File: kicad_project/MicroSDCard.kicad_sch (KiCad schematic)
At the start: 8 parts, among them J8 DM3AT, U14 ADG733BRU, U6 BD2221G-LBTR

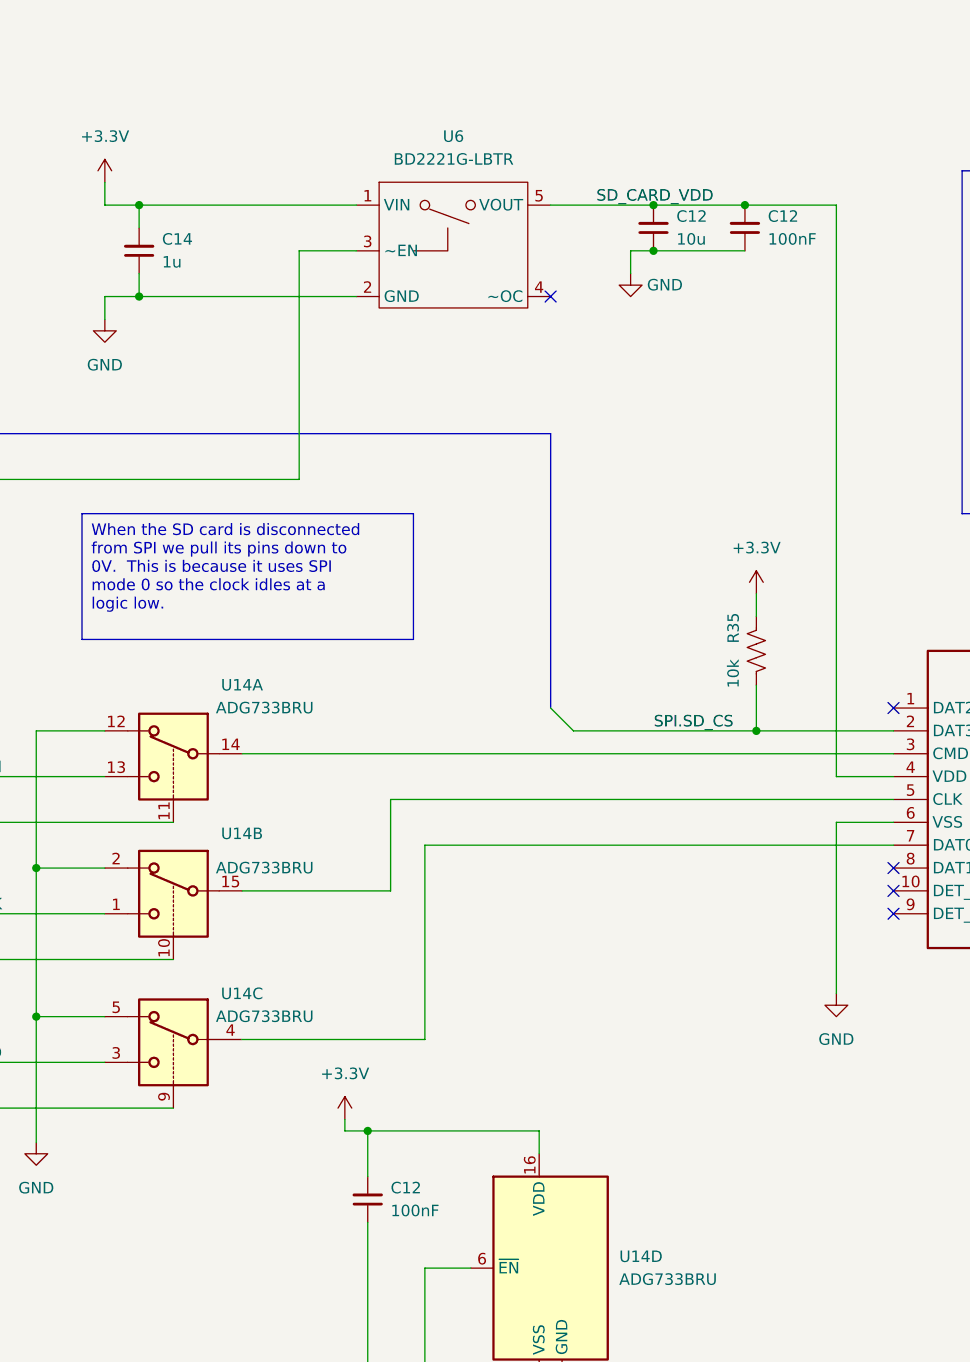
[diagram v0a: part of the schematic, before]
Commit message: Update to KiCAD 8, start adding CAN transceiver
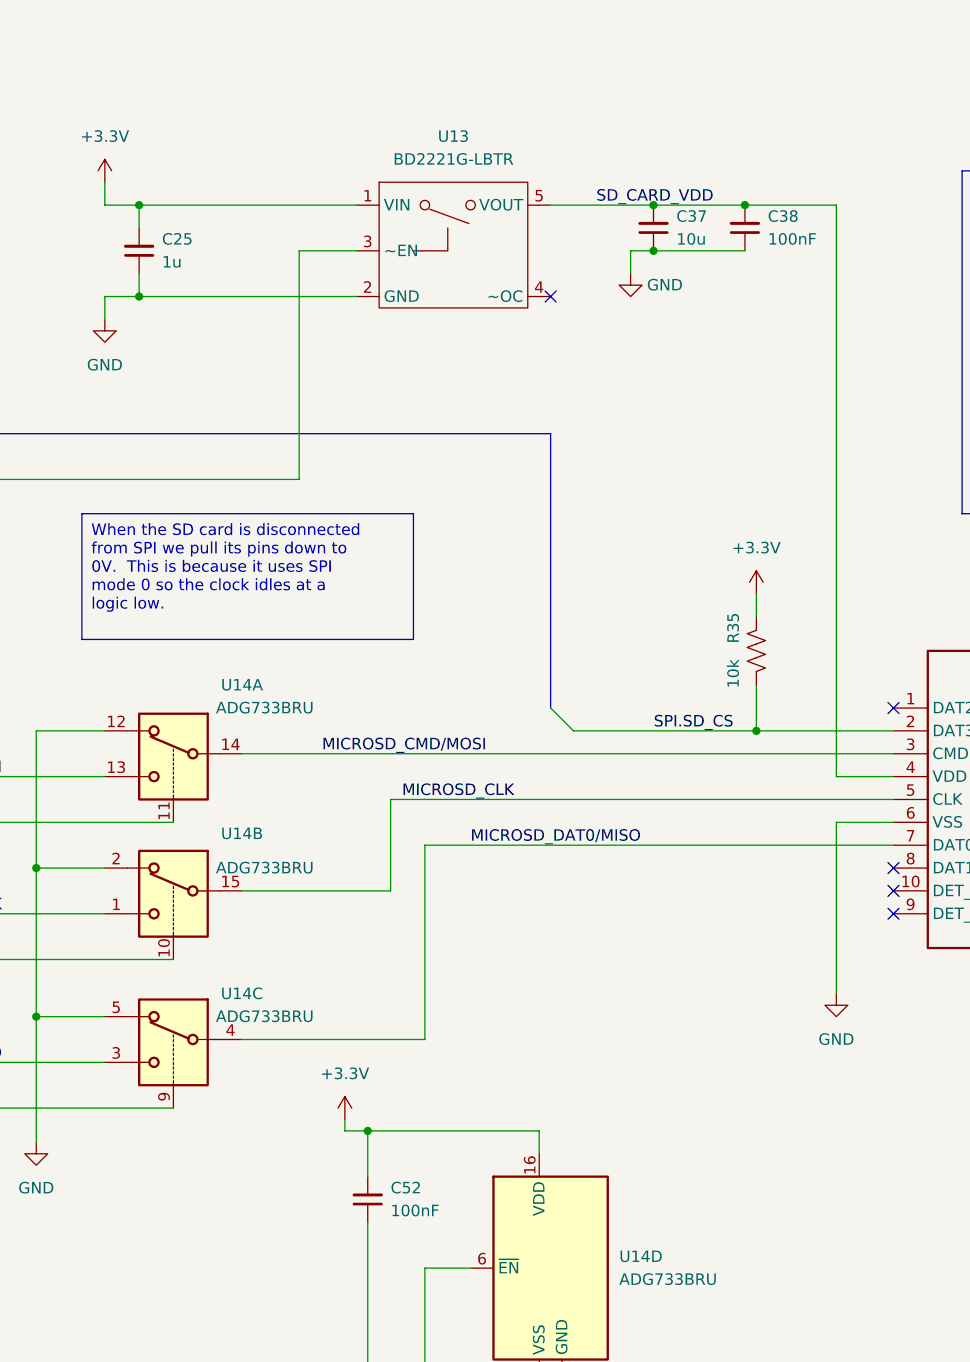
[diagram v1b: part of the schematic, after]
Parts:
- renumbered C14 to C25, C12 to C37, C12 to C38, C12 to C52, U6 to U13
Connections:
- net MICROSD_CMD/MOSI: now reaches J8.3 (CMD), U14.14
- net MICROSD_CLK: now reaches J8.5 (CLK), U14.15
- net MICROSD_DAT0/MISO: now reaches J8.7 (DAT0), U14.4

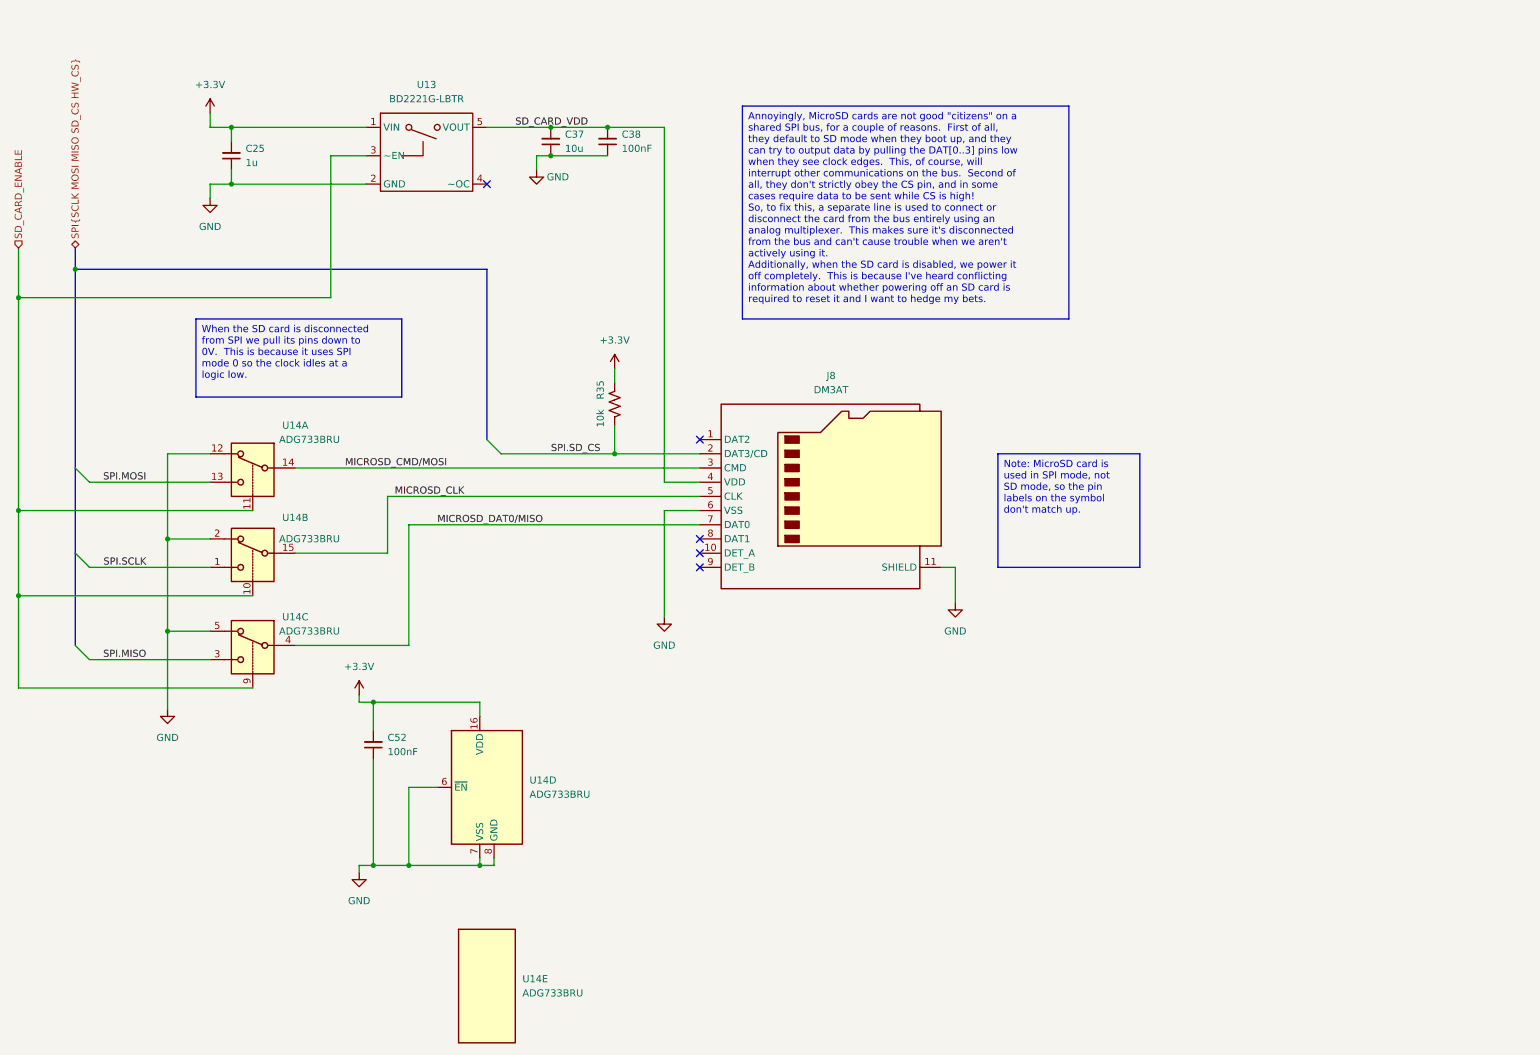
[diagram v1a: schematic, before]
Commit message: Fix all known issues with v2 r2: * Invert polarity of SD card enable line to match power switch * Decrease SPI mirror resistor resistance * Pull up SD card MISO line to 3V3 * Fix reset voltage divider to output 3.3V instead of 4V * Add diode to keep reset low while power is unplugged * Move analog in to A3 instead of A0
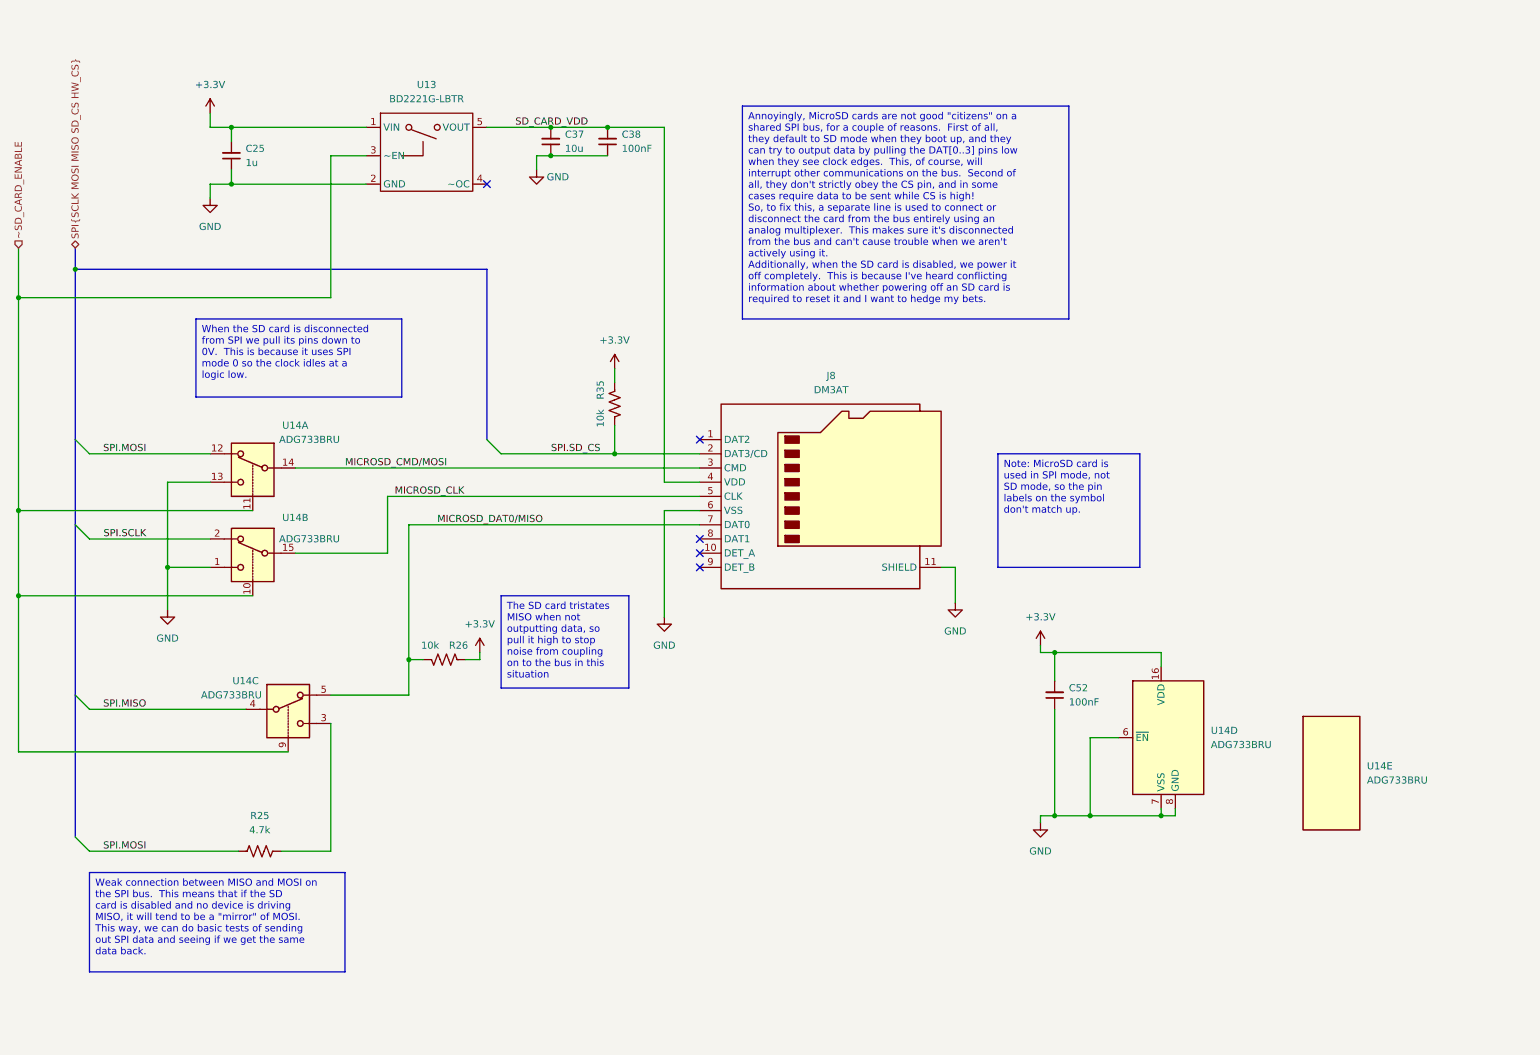
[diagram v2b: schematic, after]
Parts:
- added R25: 4.7k, Resistor_SMD:R_1206_3216Metric, symbol Device:R_US
- added R26: 10k, Resistor_SMD:R_1206_3216Metric, symbol Device:R_US
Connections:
- net +3.3V: now also R26.2
- net GND: now also U14.1, U14.13; no longer U14.12, U14.2, U14.5
- net MICROSD_DAT0/MISO: now also U14.5, R26.1; no longer U14.4
- net SPI.MISO: now also U14.4; no longer U14.3
- net SPI.MOSI: now also U14.12, R25.1; no longer U14.13
- net SPI.SCLK: now also U14.2; no longer U14.1
- net SD_CARD_ENABLE renamed ~SD_CARD_ENABLE
- new net: R25.2, U14.3
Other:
- moved on the sheet: C52, U14D, U14E

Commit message: Start adding CAN support... ~75% done with schematics
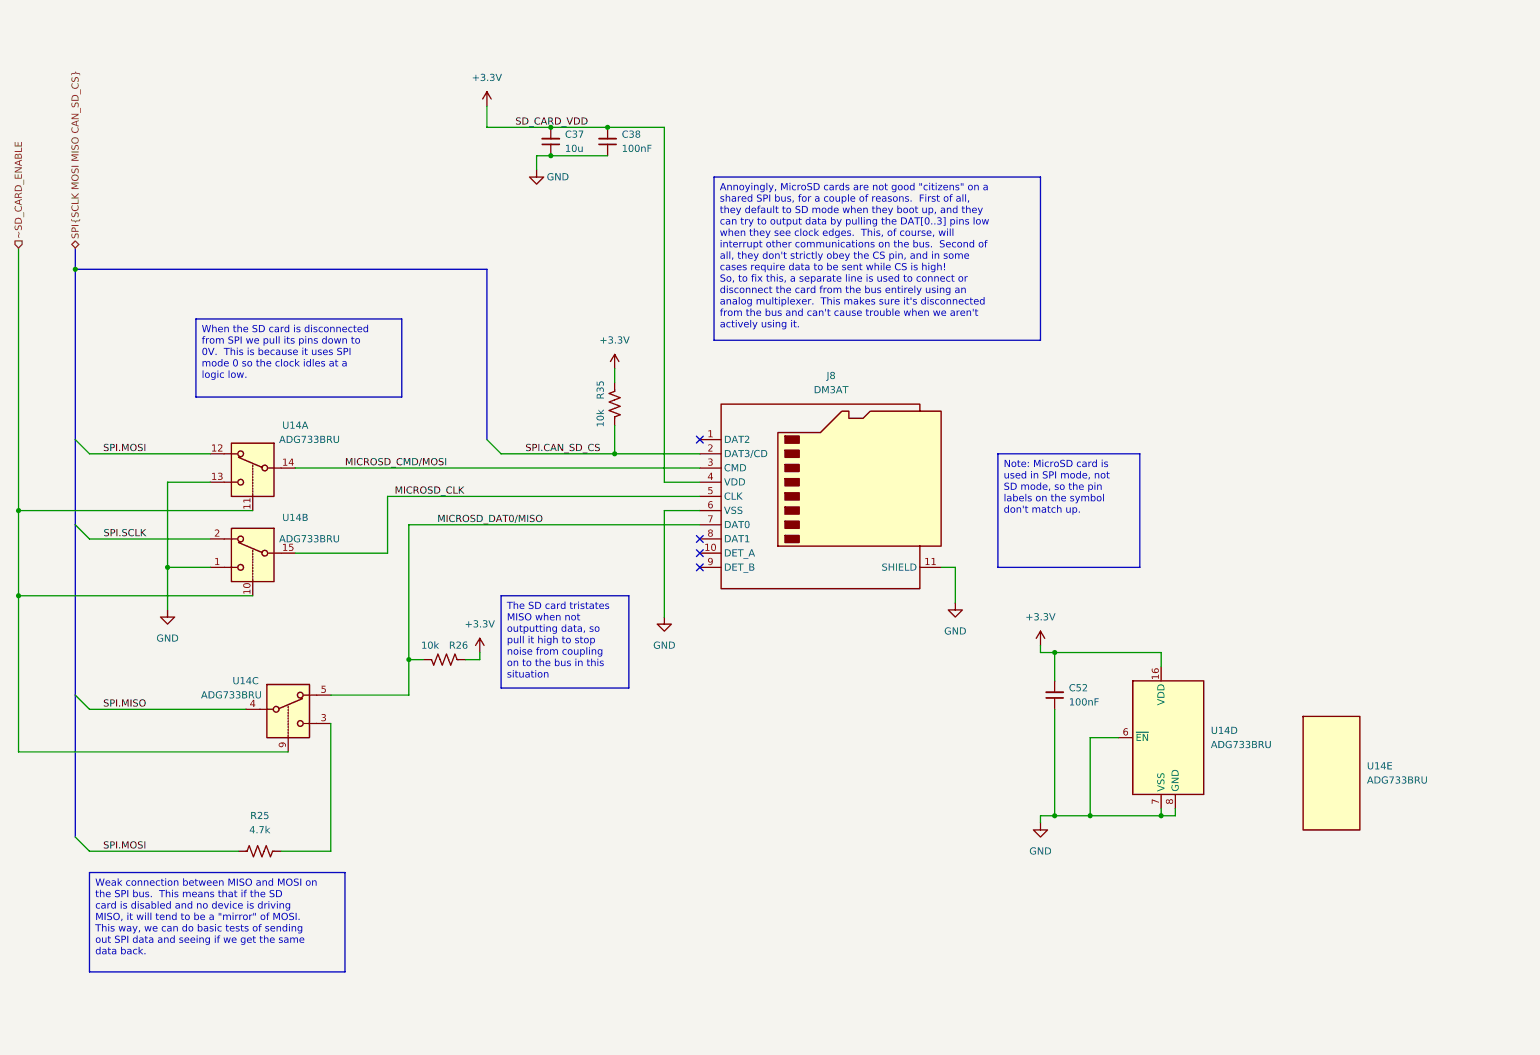
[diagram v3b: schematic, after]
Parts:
- removed C25: 1u, Capacitor_SMD:C_1206_3216Metric, symbol Device:C_Small
- removed U13: BD2221G-LBTR, Package_TO_SOT_SMD:SOT-23-5, symbol project libraries:BD2221G-LBTR
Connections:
- net SD_CARD_VDD is gone; now on net +3.3V: C37.2, C38.2, J8.4 (VDD)
- net SPI.SD_CS renamed SPI.CAN_SD_CS
- no-connect marks 5 -> 4

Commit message: ERC passing!
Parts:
- removed unit 5 of U14
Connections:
- net GND: now also U14.12, U14.2; no longer U14.1, U14.13
- net MICROSD_DAT0/MISO: now also U14.3; no longer U14.5
- net SPI.MOSI: now also U14.13; no longer U14.12
- net SPI.SCLK: now also U14.1; no longer U14.2
- net at R25.2: now also U14.5; no longer U14.3
- net ~SD_CARD_ENABLE renamed SD_CARD_ENABLE

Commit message: Kate's suggestions, part 1
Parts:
- added R56: 10k, Resistor_SMD:R_1206_3216Metric, symbol Device:R_US
- added U21: TXS0104EPW, Package_SO:TSSOP-14_4.4x5mm_P0.65mm, symbol Logic_LevelTranslator:TXS0104EPW
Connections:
- net GND: now also R56.1
- net SD_CARD_ENABLE: now also R56.2
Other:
- moved on the sheet: C52, U14D
